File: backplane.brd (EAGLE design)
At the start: 160 x 127 mm, 4 parts, among them J201 TE-2-5530843-0, J301 TE-2-5530843-0, U401 USB3150

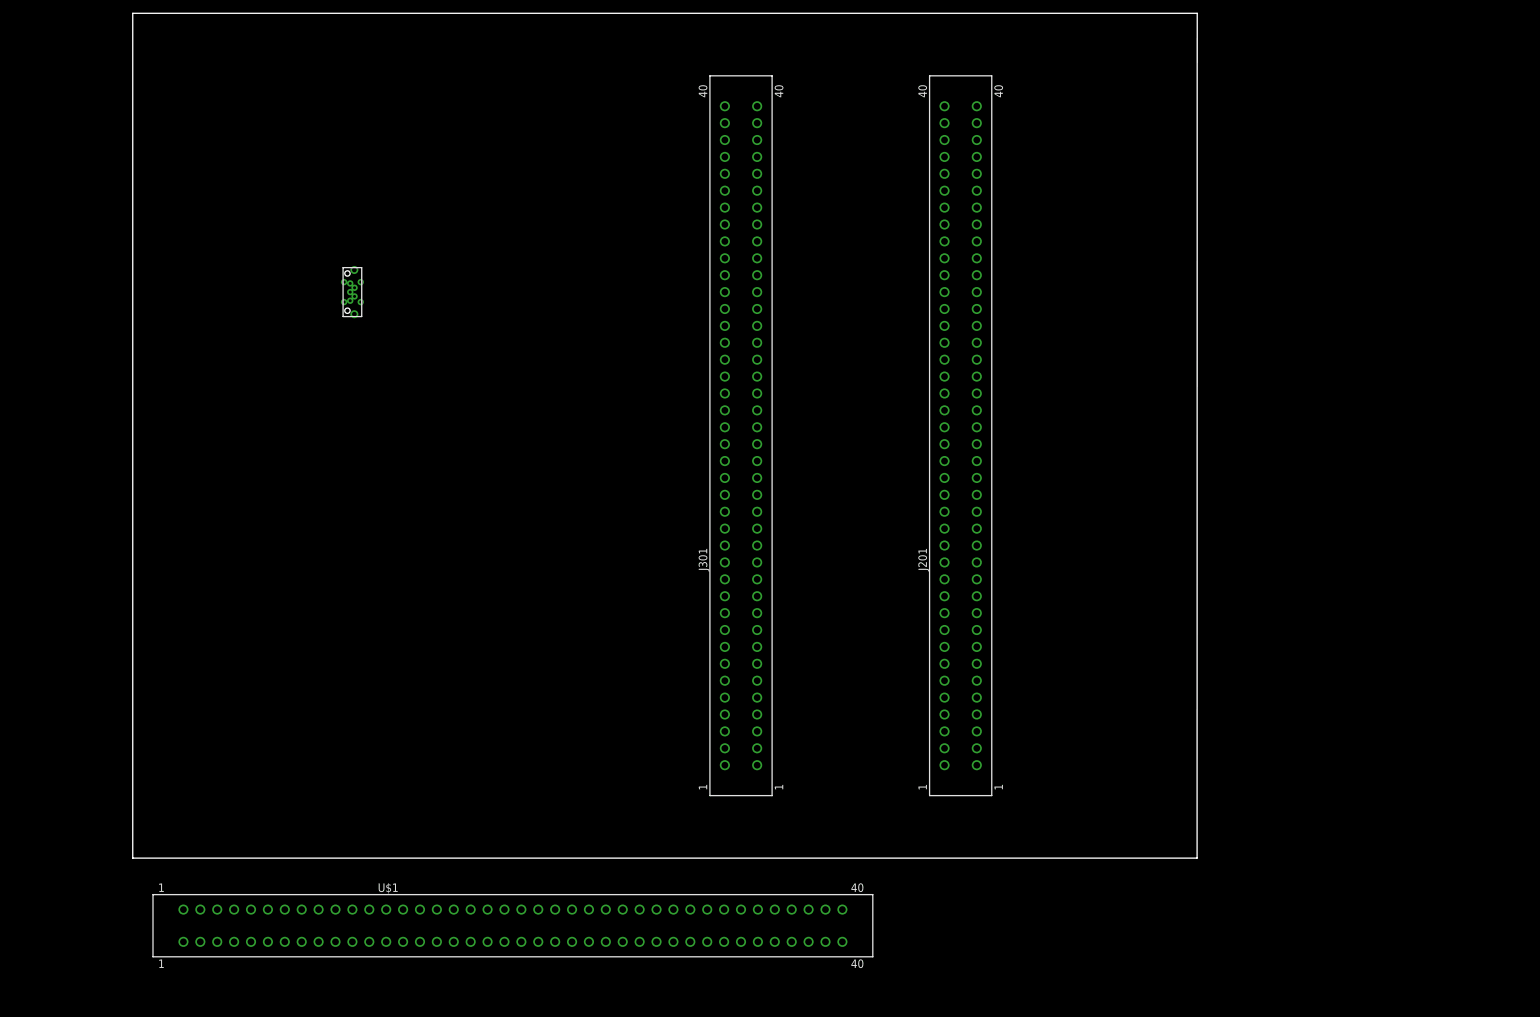
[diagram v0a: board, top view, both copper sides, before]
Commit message: Move jetson to the backplane
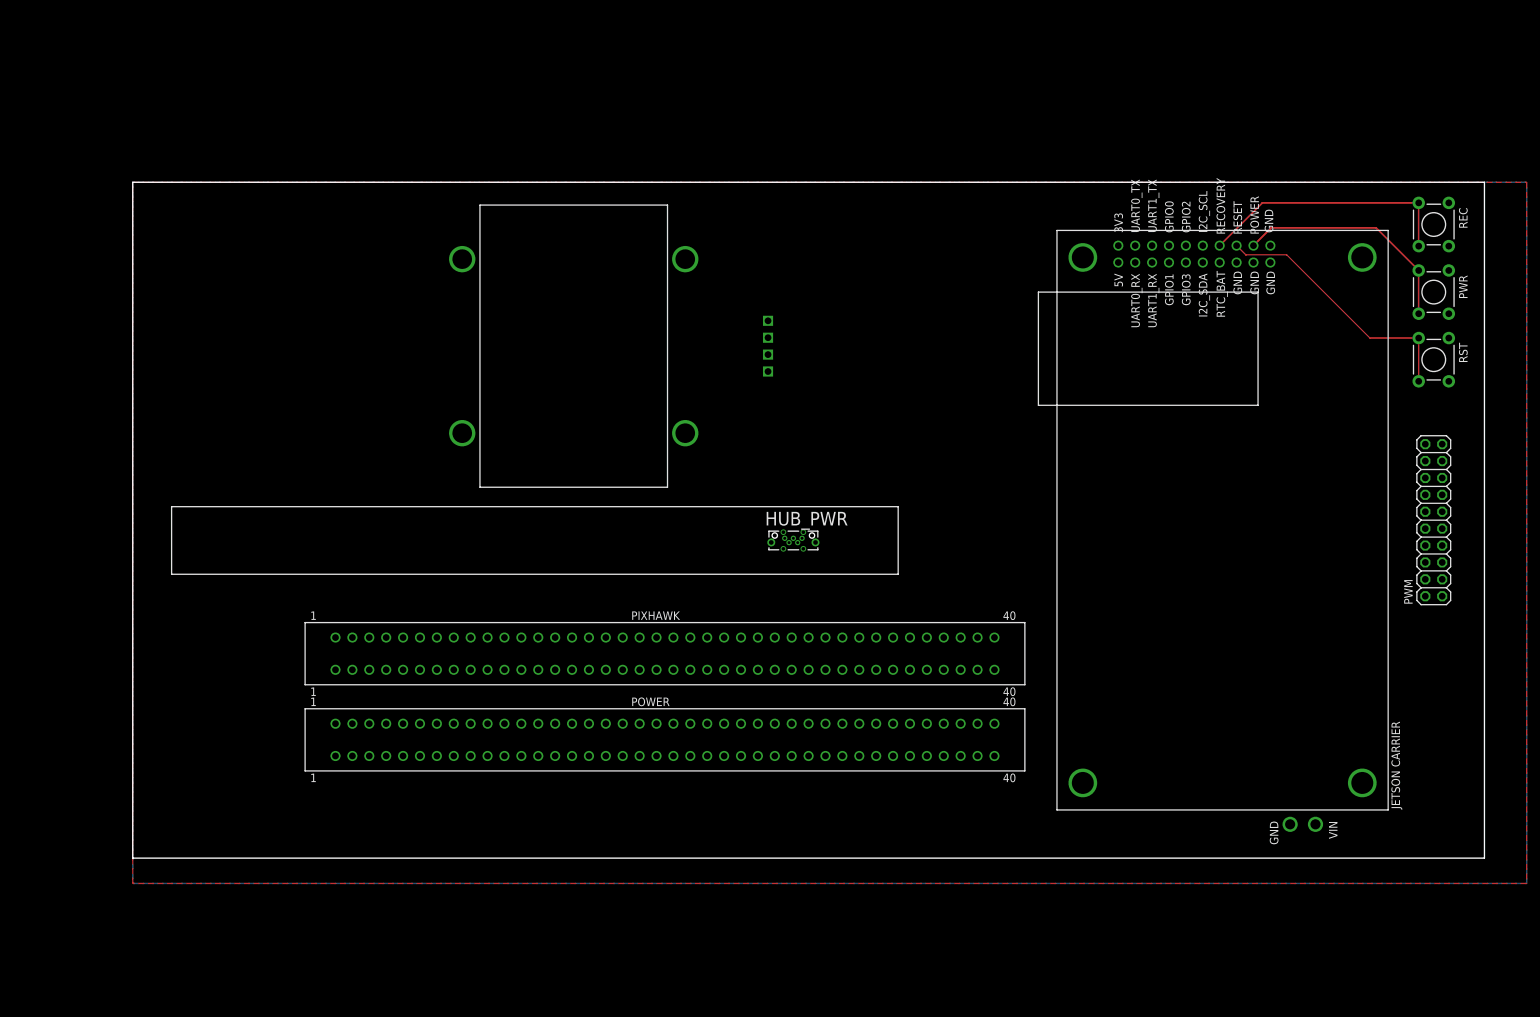
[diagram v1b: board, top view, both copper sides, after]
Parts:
- removed J201, J301: TE-2-5530843-0, auv:TE-2-5530843-0
- removed U401: USB3150, auv:USB3150
- added HUB_PWR: USB3150-30-130-A, auv:GCT_USB3150-XX-XXX-X_REVA
- added PIXHAWK, POWER: TE-2-5530843-0, auv:TE-2-5530843-0
- added PWM: (no value), auv:2X10
- added PWR, REC, RST: (no value), auv:TACTILE-PTH
- added U$3: ORBITTY_CARRIER, auv:ORBITTY_CARRIER
- U$1: value JETSON_CARRIER -> AHRS8P; device auv:TE-2-5530843-0 -> auv:AHRS8P
- moved U$1 87.6 mm to (66.3, 77.0), turned to 90 degrees
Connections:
- removed net JETSON_GPIO0: U$1.65, U$1.66
- removed net JETSON_GPIO1: U$1.63, U$1.64
- removed net JETSON_GPIO2: U$1.69, U$1.70
- removed net JETSON_GPIO3: U$1.67, U$1.68
- removed net JETSON_I2C_SCL: U$1.73, U$1.74
- removed net JETSON_I2C_SDA: U$1.71, U$1.72
- removed net JETSON_PWR_BTN: U$1.53, U$1.54
- removed net JETSON_UART1_RX: U$1.59, U$1.60
- removed net JETSON_UART1_TX: U$1.61, U$1.62
- new net +5V: HUB_PWR.1, U$1.VIN
- new net AHRS8_RX: U$1.RX
- new net AHRS8_TX: U$1.TX
- new net N$3: PWR.3, PWR.4, U$3.POWER_BUTTON
- new net N$4: RST.3, RST.4, U$3.RESET
- new net N$5: REC.3, REC.4, U$3.RECOVERY
- new net PWR: PWR.1, PWR.2
- new net SPARTON_RX: U$3.UART0_TX
- new net SPARTON_TX: U$3.UART0_RX
- net GND: now also HUB_PWR.10, HUB_PWR.11, HUB_PWR.5, HUB_PWR.6, HUB_PWR.7, HUB_PWR.8, HUB_PWR.9, PWM.1, PWM.11, PWM.13, PWM.15, PWM.17, PWM.19, PWM.3, PWM.5, PWM.7, PWM.9, REC.1, REC.2, RST.1, RST.2, U$1.GND, U$3.GND, U$3.GND1, U$3.GND2, U$3.GND3, U$3.GND4; no longer U$1.77, U$1.78, U$1.79, U$1.80
- net PIXHAWK_TELEM2_RX: now also U$3.UART1_TX; no longer U$1.57, U$1.58
- net PIXHAWK_TELEM2_TX: now also U$3.UART1_RX; no longer U$1.55, U$1.56
- net VBAT: now also U$3.VIN; no longer U$1.1, U$1.2, U$1.3, U$1.4
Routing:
- net N$4: track 0.00 -> 39.6 mm
- net N$5: track 0.00 -> 39.1 mm
- net N$3: track 0.00 -> 35.1 mm
- added copper zone on layer 16, net GND
- added copper zone on layer 1, net VBAT
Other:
- board size 160 x 127 mm -> 203.2 x 101.6 mm

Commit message: Update backplane
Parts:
- POWER: value TE-2-5530843-0 -> TE-5-5530843-0; device auv:TE-2-5530843-0 -> auv:TE-5-5530843-0
- moved POWER 49.1 mm to (31.0, 15.0)
- moved PIXHAWK 9.40 mm to (70.6, 30.5)
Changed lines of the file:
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@@
 <?xml version="1.0" encoding="utf-8"?>
 <!DOCTYPE eagle SYSTEM "eagle.dtd">
-<eagle version="8.6.3">
+<eagle version="8.7.1">
 <drawing>
 <settings>
@@
 </autorouter>
 <elements>
-<element name="POWER" library="auv" package="TE-2-5530843-0" value="TE-2-5530843-0" x="80.01" y="17.78"/>
-<element name="PIXHAWK" library="auv" package="TE-2-5530843-0" value="TE-2-5530843-0" x="80.01" y="30.734"/>
+<element name="PIXHAWK" library="auv" package="TE-2-5530843-0" value="TE-2-5530843-0" x="70.612" y="30.48"/>
 <element name="U$3" library="auv" package="ORBITTY_CARRIER" value="ORBITTY_CARRIER" x="163.83" y="50.8" rot="R90"/>
 <element name="REC" library="auv" package="TACTILE-PTH" value="" x="195.58" y="95.25" rot="R270"/>
 <element name="RST" library="auv" package="TACTILE-PTH" value="" x="195.58" y="74.93" rot="R270"/>
 <element name="PWR" library="auv" package="TACTILE-PTH" value="" x="195.58" y="85.09" rot="R270"/>
-<element name="HUB_PWR" library="auv" package="GCT_USB3150-XX-XXX-X_REVA" value="USB3150-30-130-A" x="99.314" y="47.752">
+<element name="HUB_PWR" library="auv" package="GCT_USB3150-XX-XXX-X_REVA" value="USB3150-30-130-A" x="99.314" y="47.752" smashed="yes">
 <attribute name="AVAILABILITY" value="Good" x="99.314" y="47.752" size="1.778" layer="27" display="off"/>
 <attribute name="DESCRIPTION" value=" Vertical Through Hole Type B Micro USB Plug w/ Shell Stakes and Pegs " x="99.314" y="47.752" size="1.778" layer="27" display="off"/>
 <attribute name="MF" value="Global Connector Technology" x="99.314" y="47.752" size="1.778" layer="27" display="off"/>
 <attribute name="MP" value="USB3150-30-130-A" x="99.314" y="47.752" size="1.778" layer="27" display="off"/>
+<attribute name="NAME" x="95.0486" y="50.01016875" size="2.03936875" layer="25" ratio="13" rot="SR0"/>
 <attribute name="PACKAGE" value="None" x="99.314" y="47.752" size="1.778" layer="27" display="off"/>
 <attribute name="PRICE" value="0.70 USD" x="99.314" y="47.752" size="1.778" layer="27" display="off"/>
@@
 <element name="PWM" library="auv" package="2X10" value="" x="195.58" y="50.8" rot="R90"/>
 <element name="U$1" library="auv" package="AHRS8P" value="AHRS8P" x="66.294" y="76.962" rot="R90"/>
+<element name="POWER" library="auv" package="TE-5-5530843-0" value="TE-5-5530843-0" x="30.988" y="14.986"/>
 </elements>
 <signals>
@@
 <contactref element="HUB_PWR" pad="6"/>
 <polygon width="0.1524" layer="16">
-<vertex x="209.55" y="101.6"/>
+<vertex x="203.2" y="101.6"/>
 <vertex x="0" y="101.6"/>
-<vertex x="0" y="-3.81"/>
-<vertex x="209.55" y="-3.81"/>
+<vertex x="0" y="0"/>
+<vertex x="203.2" y="0"/>
 </polygon>
 <contactref element="PWM" pad="1"/>
@@
 <polygon width="0.1524" layer="1">
 <vertex x="0" y="101.6"/>
-<vertex x="209.55" y="101.6"/>
-<vertex x="209.55" y="-3.81"/>
-<vertex x="0" y="-3.81"/>
+<vertex x="203.2" y="101.6"/>
+<vertex x="203.2" y="0"/>
+<vertex x="0" y="0"/>
 </polygon>
 </signal>

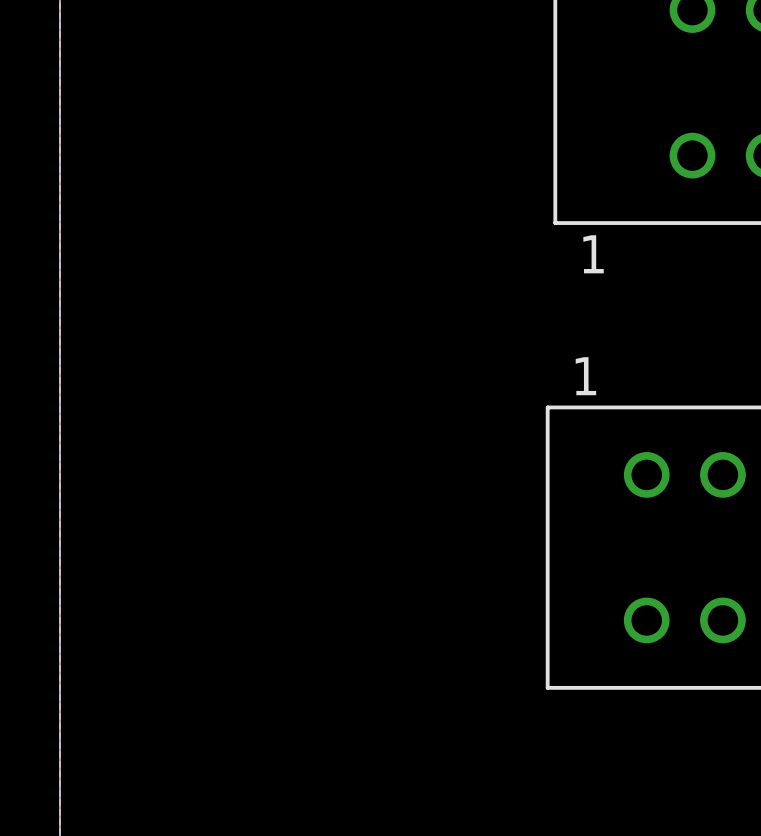
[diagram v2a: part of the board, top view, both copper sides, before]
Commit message: Add XT60 connector
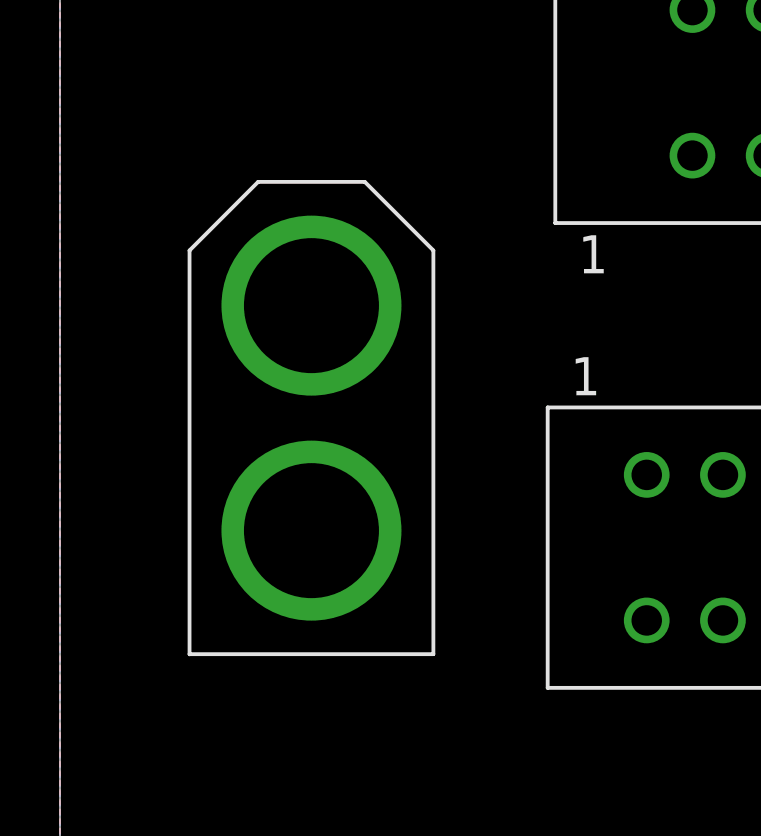
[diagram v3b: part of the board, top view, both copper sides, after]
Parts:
- added U$2: XT-60, auv:XT-60
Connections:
- net GND: now also U$2.P$2
- net VBAT: now also U$2.P$1
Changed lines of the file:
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@@
 <element name="U$1" library="auv" package="AHRS8P" value="AHRS8P" x="66.294" y="76.962" rot="R90"/>
 <element name="POWER" library="auv" package="TE-5-5530843-0" value="TE-5-5530843-0" x="30.988" y="14.986"/>
+<element name="U$2" library="auv" package="XT-60" value="XT-60" x="8.382" y="19.304" rot="R270"/>
 </elements>
 <signals>
@@
 <contactref element="PWM" pad="19"/>
 <contactref element="U$1" pad="GND"/>
+<contactref element="U$2" pad="P$2"/>
 </signal>
 <signal name="VBAT">
@@
 <vertex x="0" y="0"/>
 </polygon>
+<contactref element="U$2" pad="P$1"/>
 </signal>
 <signal name="PIXHAWK_TELEM2_TX">

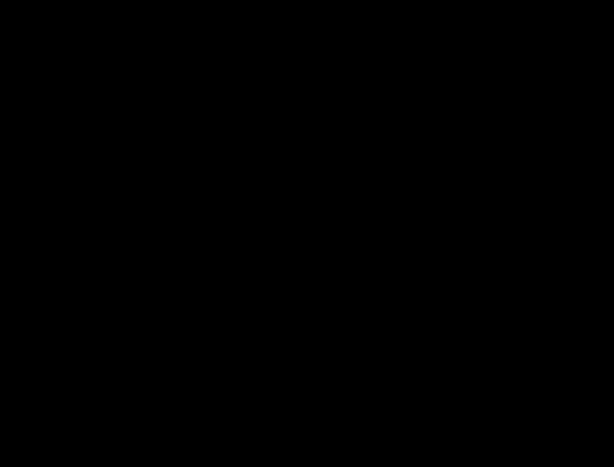
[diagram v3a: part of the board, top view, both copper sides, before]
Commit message: Depth sensor I2C
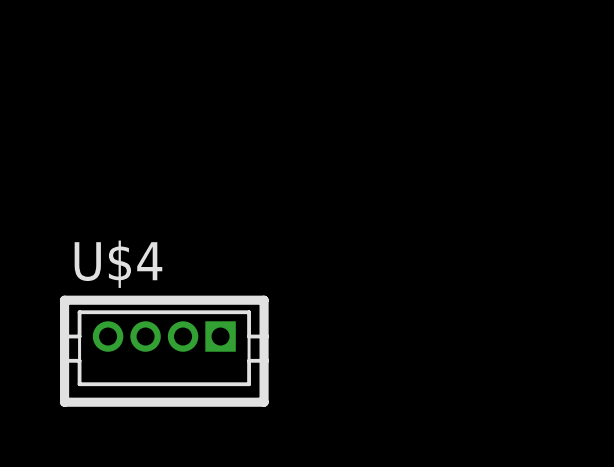
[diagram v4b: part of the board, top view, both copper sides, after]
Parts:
- added U$4: DF13-4P-1.25DSA, auv:DF13-4P-1.25DSA
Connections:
- new net 5V: U$4.P$1
- new net PIXHAWK_SCL: U$4.P$2
- new net PIXHAWK_SDA: U$4.P$3
- net GND: now also U$4.P$4
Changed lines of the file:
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@@
 <element name="POWER" library="auv" package="TE-5-5530843-0" value="TE-5-5530843-0" x="30.988" y="14.986"/>
 <element name="U$2" library="auv" package="XT-60" value="XT-60" x="8.382" y="19.304" rot="R270"/>
+<element name="U$4" library="auv" package="DF13-4P-1.25DSA" value="DF13-4P-1.25DSA" x="-14.478" y="-19.558"/>
 </elements>
 <signals>
@@
 <contactref element="U$1" pad="GND"/>
 <contactref element="U$2" pad="P$2"/>
+<contactref element="U$4" pad="P$4"/>
+<wire x1="8.382" y1="15.554" x2="-16.353" y2="-19.558" width="0" layer="19" extent="1-1"/>
 </signal>
 <signal name="VBAT">
@@
 <contactref element="U$1" pad="TX"/>
 </signal>
+<signal name="5V">
+<contactref element="U$4" pad="P$1"/>
+</signal>
+<signal name="PIXHAWK_SCL">
+<contactref element="U$4" pad="P$2"/>
+</signal>
+<signal name="PIXHAWK_SDA">
+<contactref element="U$4" pad="P$3"/>
+</signal>
 </signals>
